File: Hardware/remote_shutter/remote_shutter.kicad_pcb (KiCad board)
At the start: 2 copper layers, 16.8 x 2.2 mm, 64 parts, among them J1 Conn_01x02_Male, J2 OLED, J3 AudioJack3, J4 Buzzer, J5 USB_C_Receptacle_USB2.0, Q1 DMN2056U, Q2 DMN2056U, Q3 BC847BDW1, SW1 RotaryEncoder_Switch, SW2 RotaryEncoder_Switch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

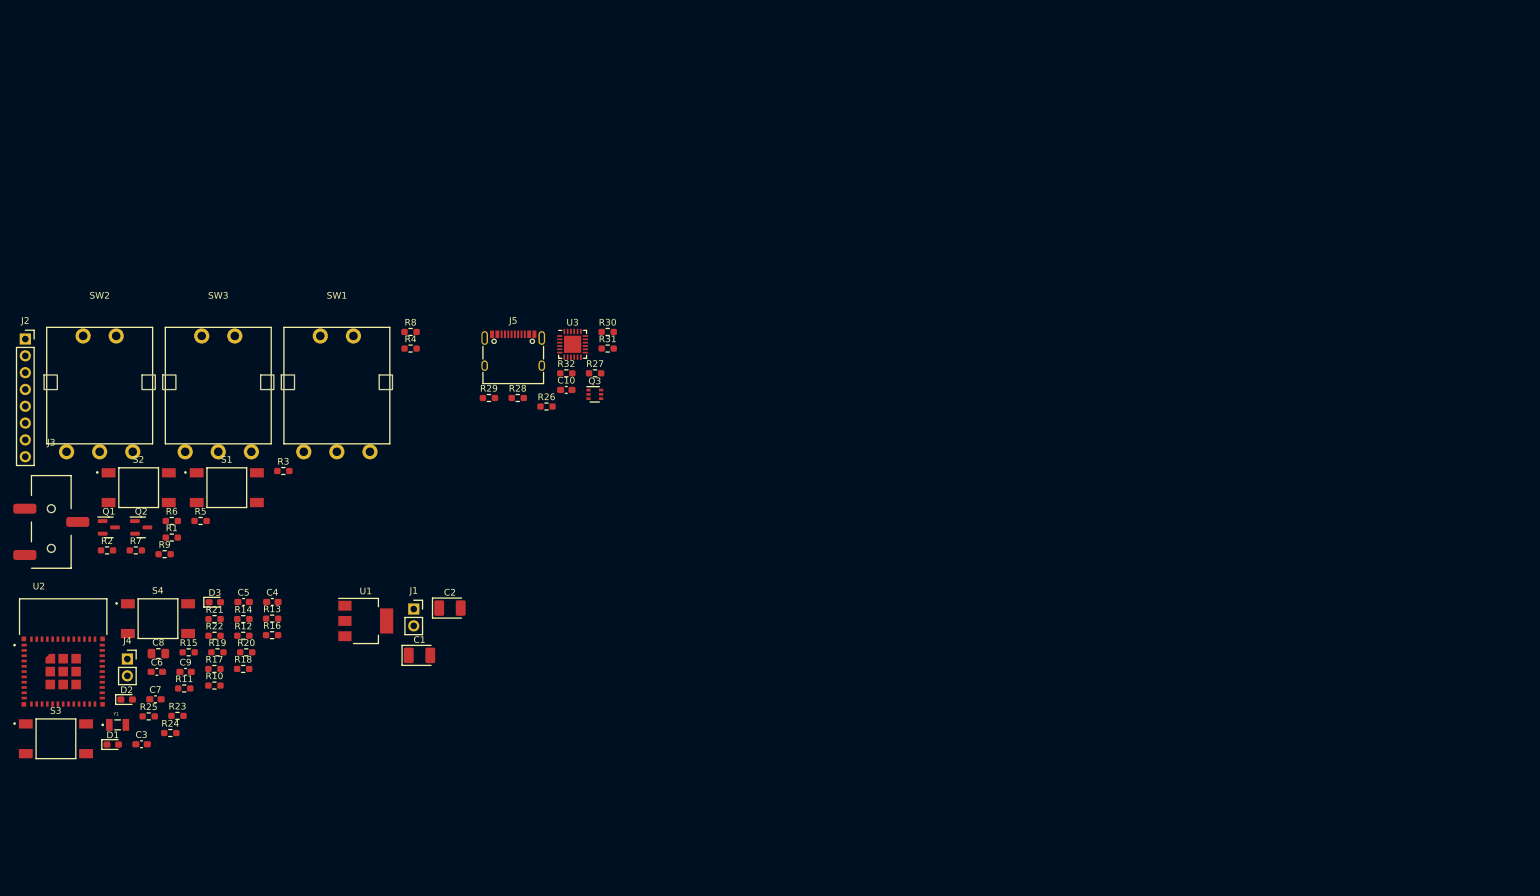
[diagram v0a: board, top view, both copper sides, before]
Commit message: Fixed bus routing
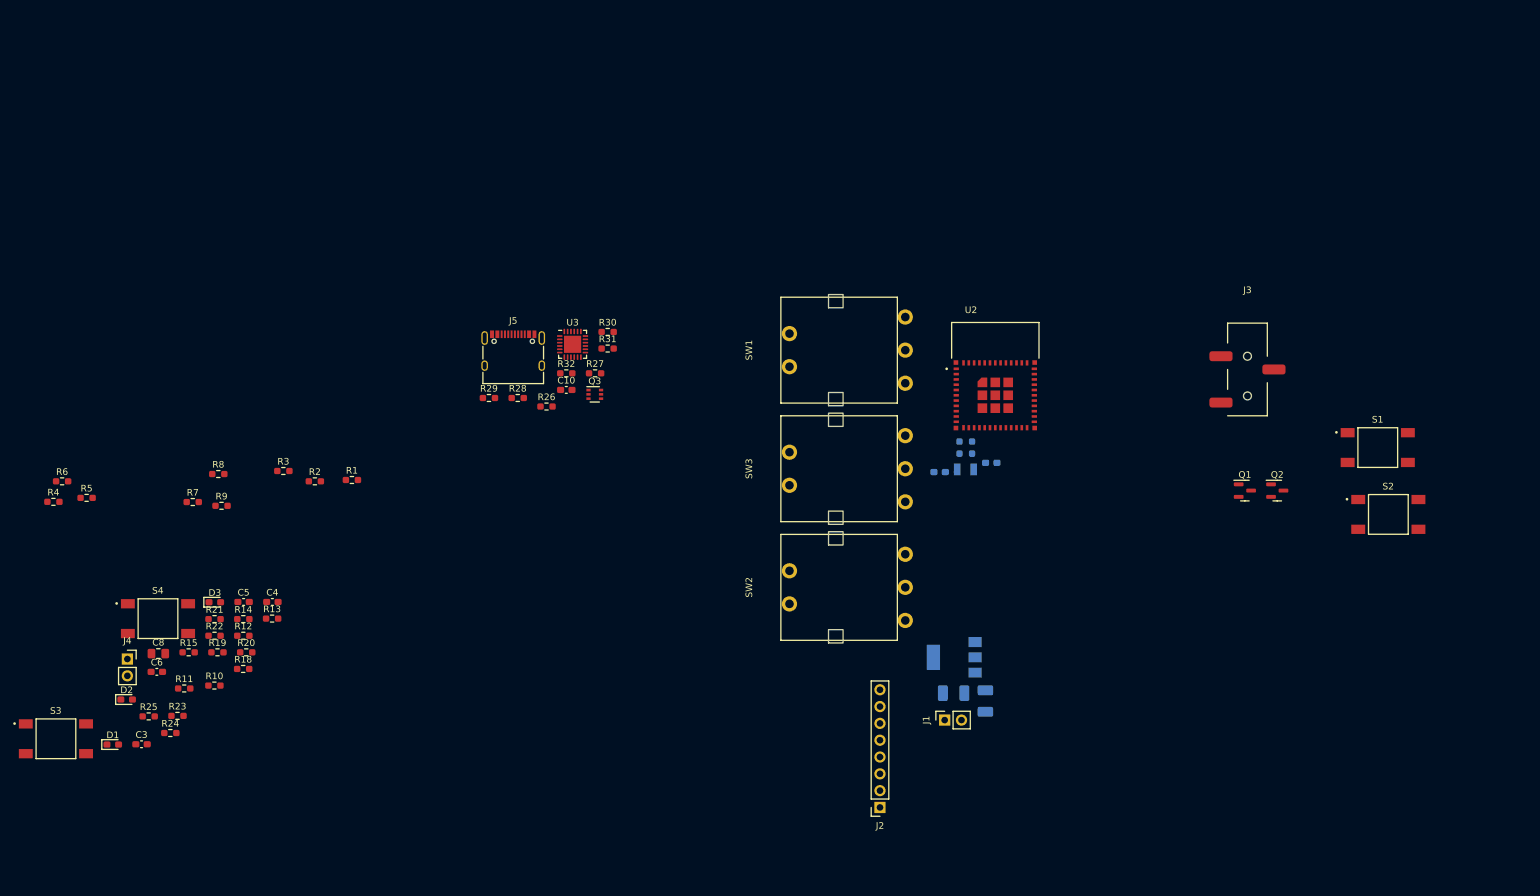
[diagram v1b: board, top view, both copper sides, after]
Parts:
- C1, C2, C7, C9, R16, R17, U1, Y1: moved to B.Cu
- moved S2 188.9 mm to (251.7, 78.0)
- moved J3 182.2 mm to (230.4, 54.1)
- moved S1 174.0 mm to (250.1, 67.9)
- moved Q2 171.7 mm to (234.9, 74.4)
- moved Q1 171.7 mm to (230.0, 74.4)
- moved J2 147.3 mm to (174.9, 122.3), turned to 180 degrees
- moved U2 146.9 mm to (192.3, 60.0)
- moved Y1 133.8 mm to (187.8, 71.2), turned to 180 degrees
- moved C9 125.8 mm to (191.7, 70.2)
- moved C7 123.4 mm to (183.9, 71.6), turned to 180 degrees
- moved R17 119.3 mm to (188.8, 67.9), turned to -90 degrees
- moved SW2 115.5 mm to (168.2, 89.0), turned to 90 degrees
- moved R16 107.7 mm to (186.9, 67.9), turned to -90 degrees
- moved SW3 94.2 mm to (168.2, 71.1), turned to 90 degrees
- moved U1 89.1 mm to (186.1, 99.6), turned to 180 degrees
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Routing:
- net Net-(C7-Pad1): track 0.00 -> 0.57 mm
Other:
- board size 16.8 x 2.2 mm -> 2.2 x 16.8 mm

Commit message: Started routing. Added power switch.
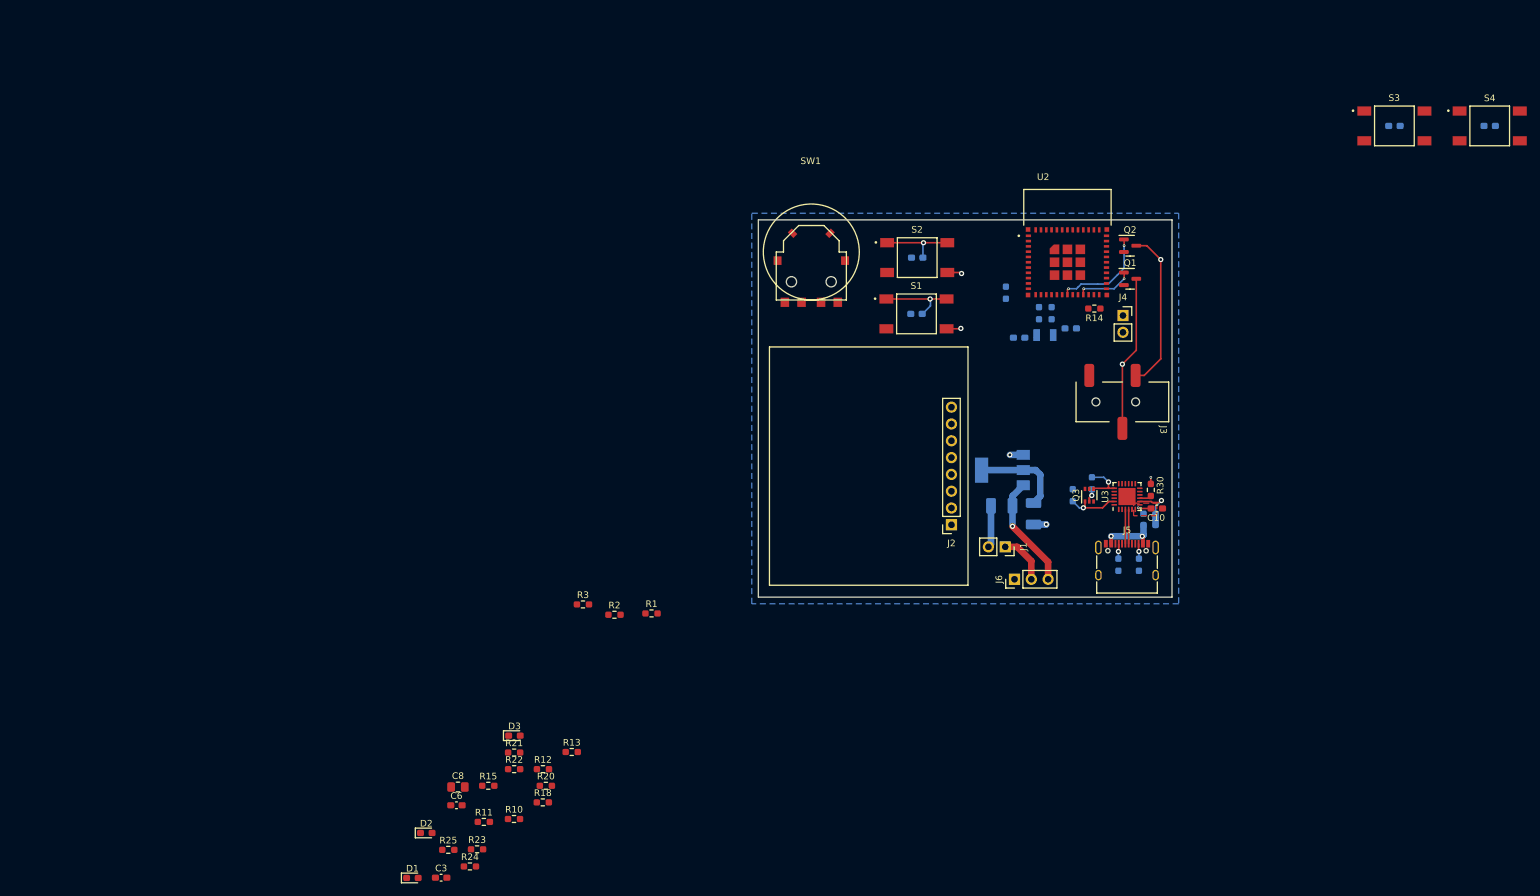
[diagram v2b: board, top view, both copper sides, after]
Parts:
- removed R4, R5, R6, R7, R8, R9: 10k, Resistor_SMD:R_0603_1608Metric_Pad0.98x0.95mm_HandSolder
- removed SW2, SW3: RotaryEncoder_Switch, footprint:PEC16
- added C11: 0u1, Capacitor_SMD:C_0603_1608Metric_Pad1.08x0.95mm_HandSolder, B.Cu at (180.4, 47.7)
- added C12: 0u1, Capacitor_SMD:C_0603_1608Metric_Pad1.08x0.95mm_HandSolder, B.Cu at (180.5, 39.2)
- added J6: Switch, Connector_PinHeader_2.54mm:PinHeader_1x03_P2.54mm_Vertical, F.Cu at (195.2, 87.8)
- C4, C5, R19, R26, R27, R28, R29, R31, R32: moved to B.Cu
- SW1: footprint footprint:PEC16 -> footprint:SIQ-02FVS3
- moved S3 222.4 mm to (252.6, 19.3)
- moved S4 214.5 mm to (267.0, 19.3)
- moved C5 201.6 mm to (267.0, 19.3)
- moved C4 184.2 mm to (252.6, 19.3)
- moved J4 159.1 mm to (211.6, 48.0)
- moved R14 136.9 mm to (207.3, 46.9), turned to 180 degrees
- moved R19 130.9 mm to (193.9, 44.5), turned to -90 degrees
- moved R29 101.3 mm to (215.6, 77.9), turned to 180 degrees
- moved J5 98.0 mm to (212.2, 86.1)
- moved R28 97.4 mm to (215.6, 79.6)
- moved R26 92.6 mm to (214.0, 85.6), turned to -90 degrees
- moved C10 91.0 mm to (216.7, 77.1)
- moved U3 86.9 mm to (212.2, 75.3), turned to 90 degrees
- moved R30 85.5 mm to (215.8, 74.3), turned to -90 degrees
- moved R27 84.2 mm to (210.9, 85.6), turned to -90 degrees
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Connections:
- net /Comms/3V3 renamed +3V3
- net /MCU/S3 renamed /MCU/C3
- J1 pad 1: Net-(C1-Pad1) -> Net-(J1-Pad1)
- R1 pad 2: /MCU/Interfaces/A1 -> /MCU/Interfaces/A0
- R19 pad 2: /MCU/A1 -> /MCU/Interfaces/A1
- R2 pad 1: /MCU/Interfaces/B1 -> /MCU/Interfaces/A1
- R20 pad 2: /MCU/A2 -> /MCU/Interfaces/A2
- R3 pad 2: /MCU/Interfaces/S1 -> /MCU/Interfaces/A2
- SW1 pad A: /MCU/Interfaces/A1 -> /MCU/Interfaces/A0
- SW1 pad B: /MCU/Interfaces/B1 -> /MCU/Interfaces/A1
- U2 pad 10: /MCU/S2 -> /MCU/B3
- U2 pad 15: /MCU/B1 -> /MCU/Interfaces/A1
- U2 pad 16: /MCU/A2 -> unconnected-(U2-Pad16)
- U2 pad 17: /MCU/B2 -> unconnected-(U2-Pad17)
- U2 pad 34: /MCU/A1 -> /MCU/Interfaces/A0
- U2 pad 9: /MCU/S1 -> /MCU/A3
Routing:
- net /MCU/Interfaces/SHUTTER: track 0.00 -> 61.5 mm, vias 0 -> 2
- net /MCU/Interfaces/FOCUS: track 0.00 -> 52.3 mm, vias 0 -> 2
- net GND: track 0.00 -> 33.6 mm, vias 0 -> 4
- net Net-(C1-Pad1): track 0.00 -> 17.1 mm, vias 0 -> 1
- net +3V3: track 0.00 -> 16.8 mm, vias 0 -> 2
- net /MCU/STRIG: track 0.00 -> 15.0 mm, vias 0 -> 2
- net Net-(J5-PadA4): track 0.00 -> 11.2 mm, vias 0 -> 2
- net /MCU/FTRIG: track 0.00 -> 8.61 mm, vias 0 -> 2
- net /Comms/DTR: track 0.00 -> 8.12 mm, vias 0 -> 1
- net Net-(J1-Pad1): track 0.00 -> 7.59 mm
- net Net-(R28-Pad2): track 0.00 -> 7.52 mm, vias 0 -> 1
- net /Comms/RTS: track 0.00 -> 6.92 mm, vias 0 -> 1
- net /Comms/DP: track 0.00 -> 5.19 mm
- net /Comms/DN: track 0.00 -> 5.19 mm
- net Net-(J5-PadB5): track 0.00 -> 2.28 mm, vias 0 -> 1
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- added copper zone on B.Cu, net +3V3
- added copper zone on F.Cu, net +3V3
- added copper zone on In2.Cu, net GND
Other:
- board size 2.2 x 16.8 mm -> 62.5 x 57 mm
- copper layers 2 -> 4

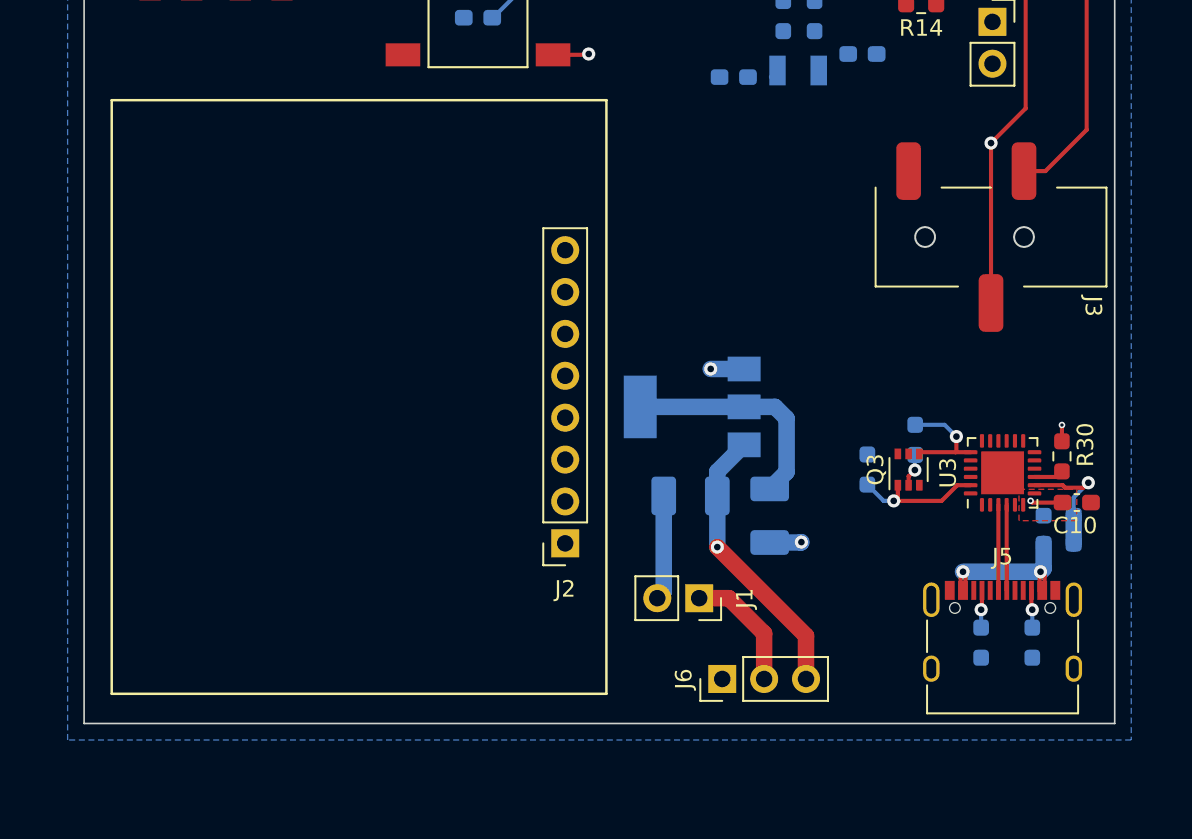
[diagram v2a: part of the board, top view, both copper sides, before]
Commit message: Routing USB and charger.
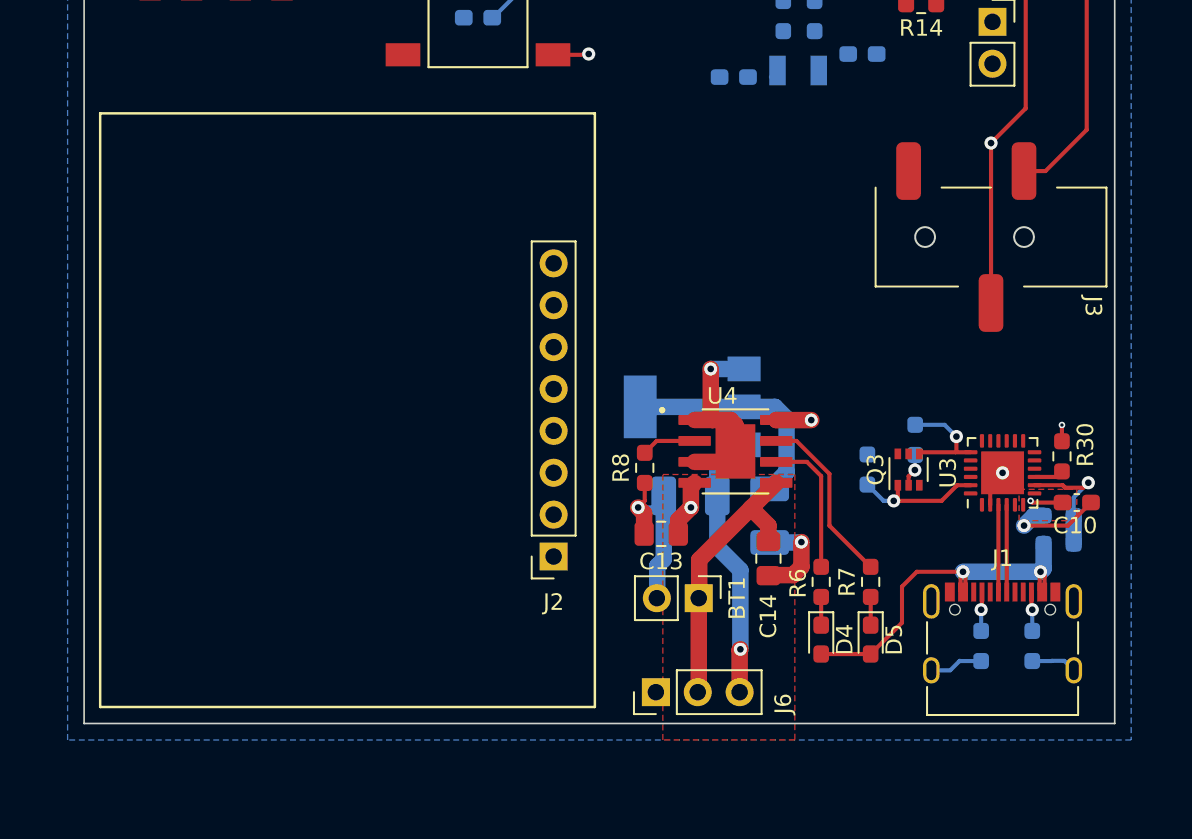
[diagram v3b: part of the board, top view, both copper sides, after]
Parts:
- removed J5: USB_C_Receptacle_USB2.0, Connector_USB:USB_C_Receptacle_XKB_U262-16XN-4BVC11
- removed R26, R27: 5k1, Resistor_SMD:R_0603_1608Metric_Pad0.98x0.95mm_HandSolder
- added BT1: 18650, Connector_PinHeader_2.54mm:PinHeader_1x02_P2.54mm_Vertical, F.Cu at (193.8, 82.9)
- added C13: 10u, Capacitor_SMD:C_0805_2012Metric_Pad1.18x1.45mm_HandSolder, F.Cu at (191.5, 79.0)
- added C14: 10u, Capacitor_SMD:C_0805_2012Metric_Pad1.18x1.45mm_HandSolder, F.Cu at (198.0, 80.5)
- added D4: GREEN, LED_SMD:LED_0603_1608Metric_Pad1.05x0.95mm_HandSolder, F.Cu at (201.2, 85.4)
- added D5: RED, LED_SMD:LED_0603_1608Metric_Pad1.05x0.95mm_HandSolder, F.Cu at (204.2, 85.4)
- added R4: 5k1, Resistor_SMD:R_0603_1608Metric_Pad0.98x0.95mm_HandSolder, B.Cu at (214.0, 85.8)
- added R5: 5k1, Resistor_SMD:R_0603_1608Metric_Pad0.98x0.95mm_HandSolder, B.Cu at (210.9, 85.8)
- added R6: 1k, Resistor_SMD:R_0603_1608Metric_Pad0.98x0.95mm_HandSolder, F.Cu at (201.2, 81.9)
- added R7: 1k, Resistor_SMD:R_0603_1608Metric_Pad0.98x0.95mm_HandSolder, F.Cu at (204.2, 81.9)
- added R8: 1k33, Resistor_SMD:R_0603_1608Metric_Pad0.98x0.95mm_HandSolder, F.Cu at (190.5, 75.0)
- added U4: TP4056, footprint:SOP127P600X175-9N, F.Cu at (196.0, 74.0)
- J1: value Conn_01x02_Male -> USB_C_Receptacle_USB2.0; footprint Connector_PinSocket_2.54mm:PinSocket_1x02_P2.54mm_Vertical -> Connector_USB:USB_C_Receptacle_XKB_U262-16XN-4BVC11
- moved J1 18.7 mm to (212.2, 86.2), turned to 0 degrees
- moved J6 4.10 mm to (191.2, 88.6)
- moved J2 1.06 mm to (185.0, 80.4)
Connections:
- J6 pad 2: Net-(J1-Pad1) -> /Power/VBAT
- R28 pad 1: Net-(J5-PadA4) -> /VBUS
- U3 pad 3: /Comms/DP -> /DP
- U3 pad 4: /Comms/DN -> /DN
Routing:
- net /VBUS: track 0.00 -> 52.2 mm, vias 0 -> 4
- net GND: track 33.6 -> 67.0 mm, vias 4 -> 7
- net /Power/VBAT: track 0.00 -> 17.1 mm
- net Net-(J5-PadA4): track 11.2 -> 0.00 mm, vias 2 -> 0
- net Net-(R7-Pad2): track 0.00 -> 10.7 mm
- net Net-(R6-Pad2): track 0.00 -> 8.58 mm
- net Net-(J1-Pad1): track 7.59 -> 0.00 mm
- net /DP: track 0.00 -> 5.19 mm
- net /DN: track 0.00 -> 5.19 mm
- net /Comms/DP: track 5.19 -> 0.00 mm
- net /Comms/DN: track 5.19 -> 0.00 mm
- net Net-(R8-Pad2): track 0.00 -> 3.32 mm
- net Net-(J5-PadB5): track 2.28 -> 0.00 mm, vias 1 -> 0
- net Net-(J1-PadB5): track 0.00 -> 2.28 mm, vias 0 -> 1
- net Net-(J5-PadA5): track 2.28 -> 0.00 mm, vias 1 -> 0
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- added copper zone on F.Cu, net /Power/VBAT
- added copper zone on In1.Cu, net /VBUS
